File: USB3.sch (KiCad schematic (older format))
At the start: 95 parts

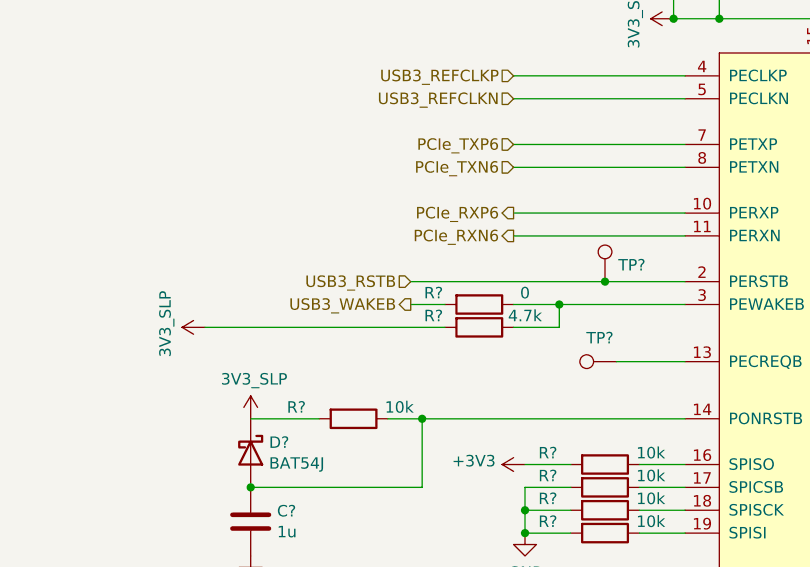
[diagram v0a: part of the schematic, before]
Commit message: fix Reset signal path
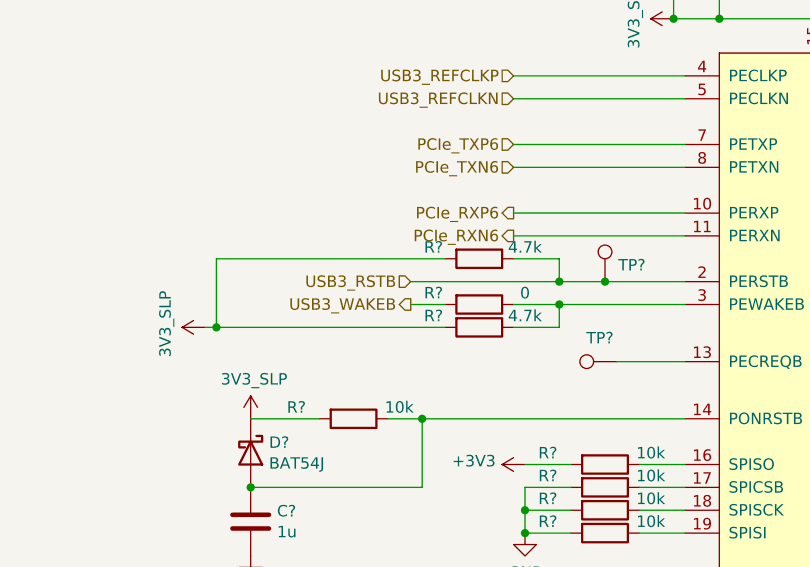
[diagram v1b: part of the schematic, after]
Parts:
- added R?: 4.7k, symbol Device:R
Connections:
- net 3V3_SLP: now also R?.2
- net USB3_RSTB: now also R?.1
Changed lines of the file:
@@
 $Descr A3 16535 11693
 encoding utf-8
-Sheet 19 28
+Sheet 18 28
 Title "DJANGO"
 Date "2020-12-06"
@@
 $EndComp
 Wire Wire Line
-	4500 3550 5350 3550
+	4500 3550 5150 3550
 Wire Wire Line
 	4650 3650 4500 3650
@@
 $EndComp
 Wire Wire Line
-	3600 3750 4650 3750
+	3600 3750 3650 3750
 $Comp
 L ppc_scm:3V3_SLP #PWR?
@@
 $EndComp
 Connection ~ 900  9500
+$Comp
+L Device:R R?
+U 1 1 60855813
+P 4800 3450
+F 0 "R?" V 4750 3250 50  0000 C CNN
+F 1 "4.7k" V 4750 3650 50  0000 C CNN
+F 2 "" V 4730 3450 50  0001 C CNN
+F 3 "~" H 4800 3450 50  0001 C CNN
+	1    4800 3450
+	0    1    1    0
+$EndComp
+Wire Wire Line
+	4950 3450 5150 3450
+Wire Wire Line
+	5150 3450 5150 3550
+Connection ~ 5150 3550
+Wire Wire Line
+	5150 3550 5350 3550
+Wire Wire Line
+	4650 3450 3650 3450
+Wire Wire Line
+	3650 3450 3650 3750
+Connection ~ 3650 3750
+Wire Wire Line
+	3650 3750 4650 3750
 $EndSCHEMATC
